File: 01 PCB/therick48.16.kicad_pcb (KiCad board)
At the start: 2 copper layers, 308.9 x 75.8 mm, 173 parts, among them J1 TYPE-C-31-M12_13, J2 AVR-ISP-6_mod, K1 KEYSW, K10 KEYSW, K11 KEYSW, K12 KEYSW, K13 KEYSW, K14 KEYSW, K15 KEYSW, K16 KEYSW, K17 KEYSW, K18 KEYSW, K19 KEYSW, K2 KEYSW, K20 KEYSW, K21 KEYSW, K22 KEYSW, K23 KEYSW, K24 KEYSW, K25 KEYSW, K26 KEYSW, K27 KEYSW, K28 KEYSW, K29 KEYSW, K3 KEYSW, K30 KEYSW, K31 KEYSW, K32 KEYSW, K33 KEYSW, K34 KEYSW, K35 KEYSW, K36 KEYSW, K37 KEYSW, K38 KEYSW, K39 KEYSW, K4 KEYSW, K40 KEYSW, K41 KEYSW, K42 KEYSW, K43 KEYSW, K44 KEYSW, K45 KEYSW, K46 KEYSW, K47 KEYSW, K48 KEYSW, K49 KEYSW, K5 KEYSW, K50 KEYSW, K51 KEYSW, K52 KEYSW, K53 KEYSW, K54 KEYSW, K55 KEYSW, K56 KEYSW, K57 KEYSW, K58 KEYSW, K59 KEYSW, K6 KEYSW, K60 KEYSW, K61 KEYSW, K62 KEYSW, K63 KEYSW, K64 KEYSW, K7 KEYSW, K8 KEYSW, K9 KEYSW, SW1 SW_PUSH, U1 ATMEGA32U4, U2 HOLE, U3 USBLC6-2SC6, U4 HOLE, U5 HOLE, U6 HOLE, U7 HOLE, U8 HOLE, Y1 16MHz

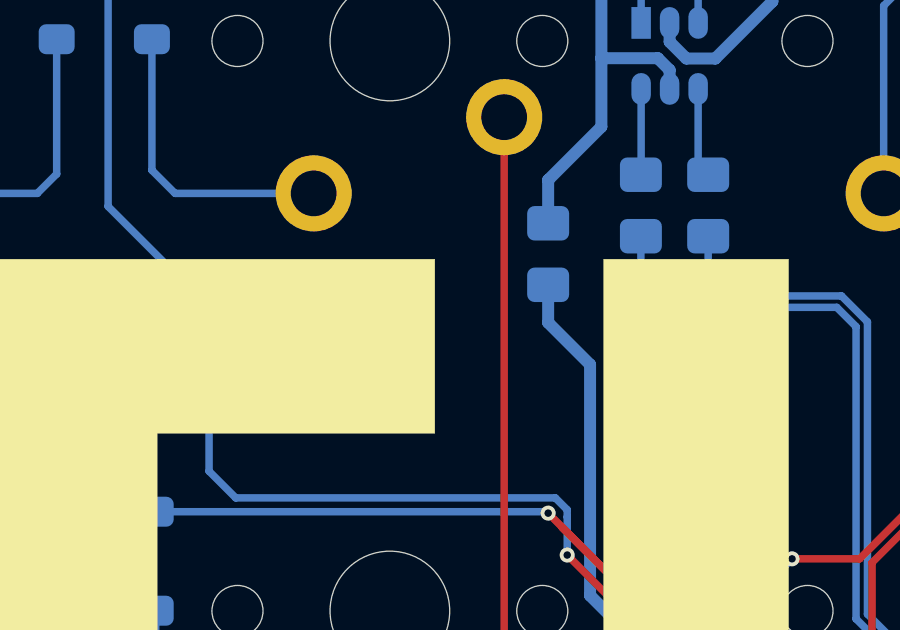
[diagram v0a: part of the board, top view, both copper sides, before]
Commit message: Add Power LED
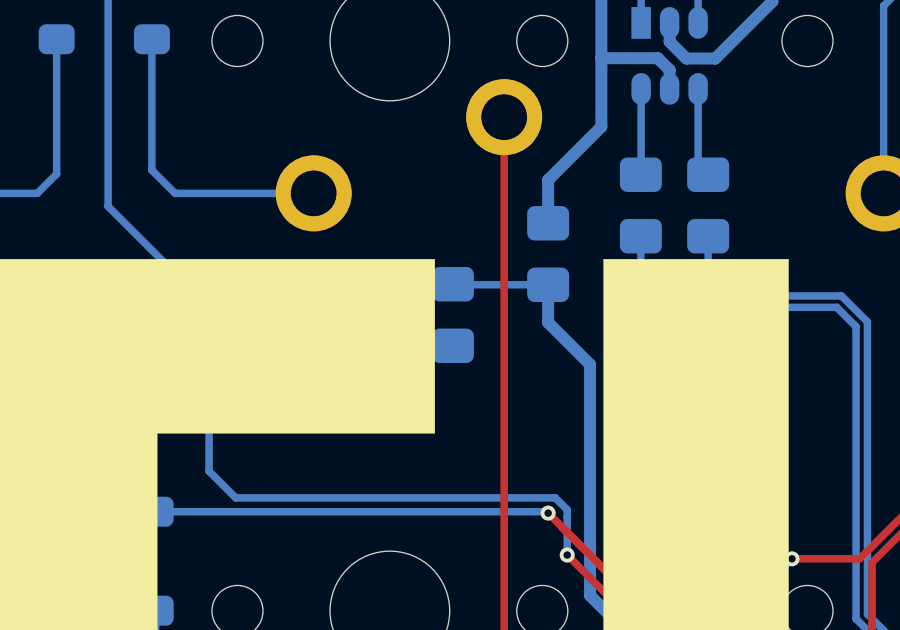
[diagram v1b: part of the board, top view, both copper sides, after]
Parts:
- added LED1: LED, LED_SMD:LED_0805_2012Metric_Pad1.15x1.40mm_HandSolder, B.Cu at (73.8, 53.6)
- added R4: 1K, Resistor_SMD:R_0805_2012Metric_Pad1.15x1.40mm_HandSolder, B.Cu at (76.6, 53.6)
- added U9: HOLE, Symbol:OSHW-Logo2_9.8x8mm_SilkScreen, B.Cu at (55.0, 93.7)
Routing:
- net VCC: track 215.1 -> 218.3 mm
- net Net-(LED1-Pad2): track 0.00 -> 2.79 mm
